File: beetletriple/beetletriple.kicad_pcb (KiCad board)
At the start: 4 copper layers, 80 x 70 mm, 65 parts, among them J1 Power IN, J2 motor_out, J3 motor_out, J4 motor_out, J5 input_c1, J6 input_c2, J7 input_c3, Q1 IRF8313PBF, Q2 IRF8313PBF, Q3 IRF8313PBF, Q4 IRF8313PBF, Q5 IRF8313PBF, Q6 IRF8313PBF, U1 LM2596S-ADJ, U11 FAN7388MX, U12 FAN7388MX, U2 HT7550-1, U3 ATtiny1617-M

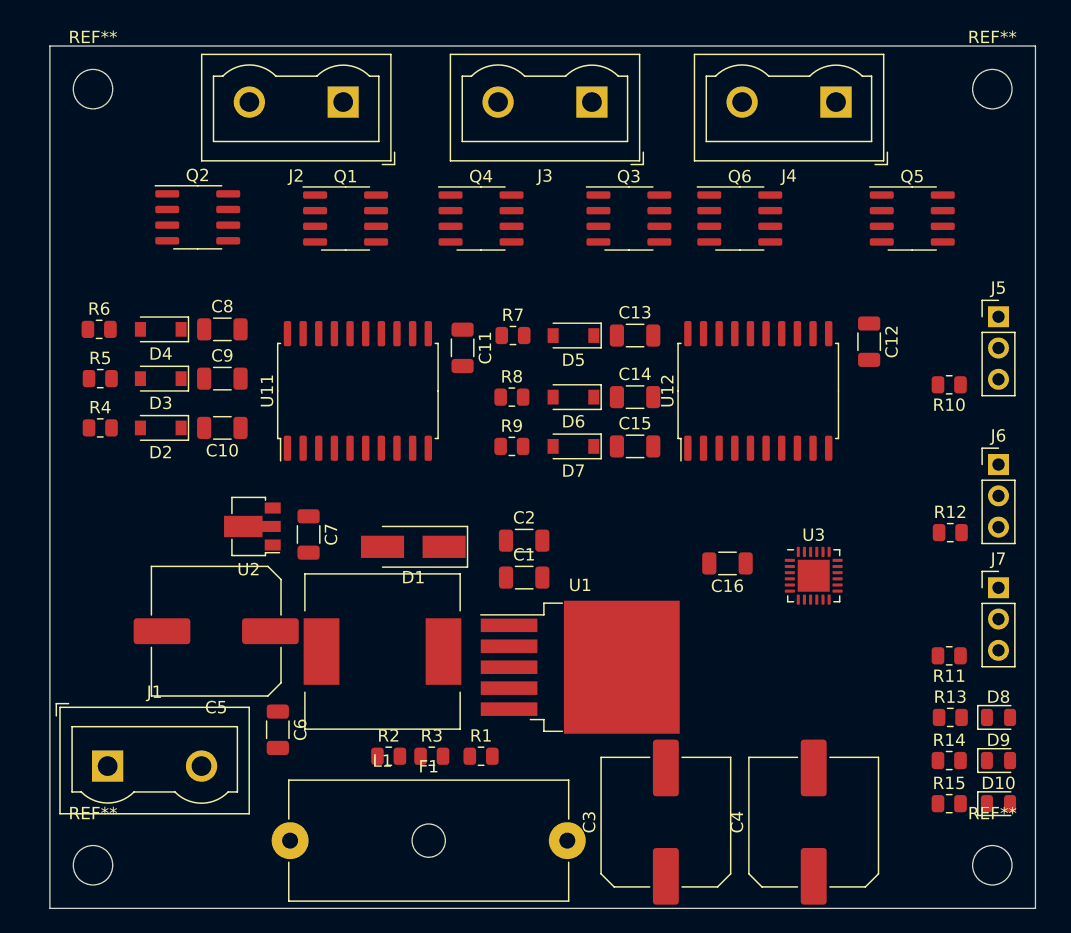
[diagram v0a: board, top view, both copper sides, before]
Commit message: Beetleweight triple esc
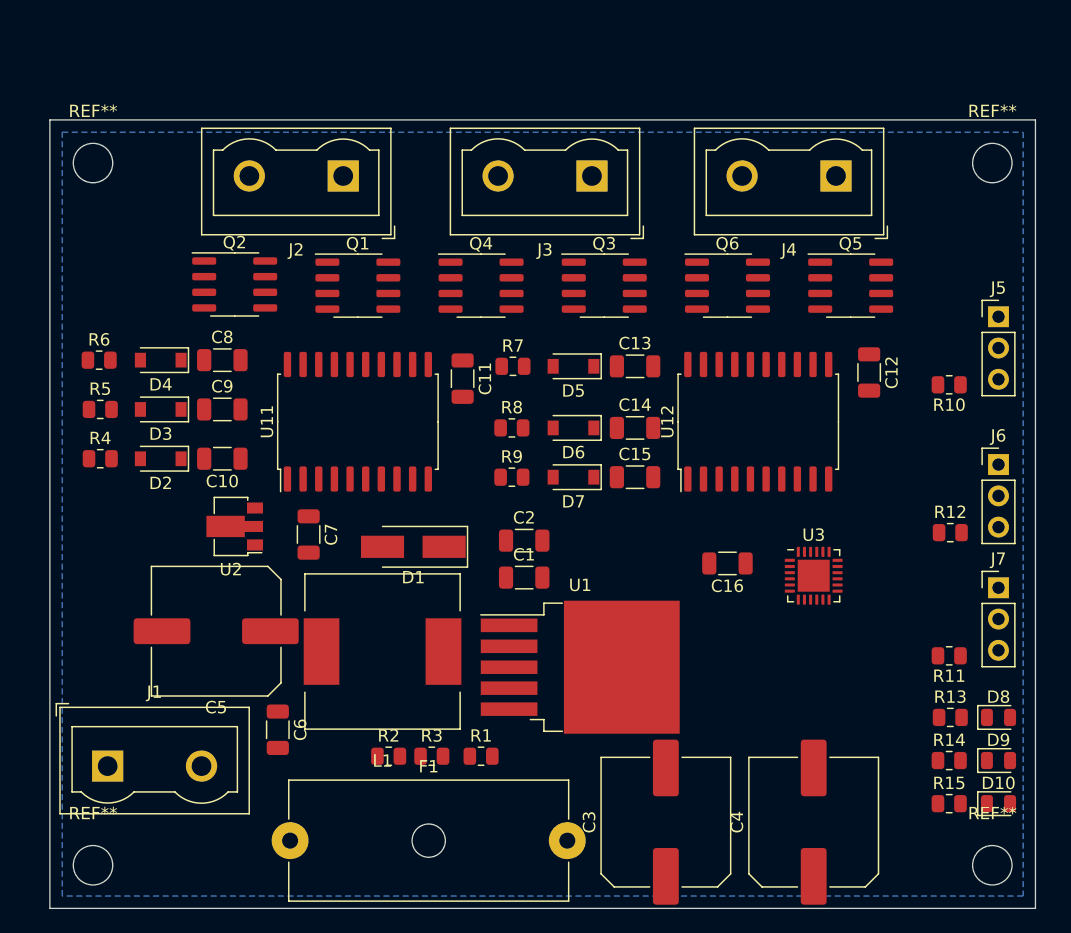
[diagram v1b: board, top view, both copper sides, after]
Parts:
- C10, C13, C14, C15, C8, C9: value C -> 2.2uF 50V
- C11, C12, C16: value 1uF 50V -> 2.2uF 50V
- R4, R5, R6, R7, R8, R9: value R -> 4.7R
- moved Q5 7.40 mm to (163.0, 89.5)
- moved Q2 6.22 mm to (113.0, 89.4)
- moved J2 6.00 mm to (121.8, 80.5)
- moved J3 6.00 mm to (142.0, 80.5)
- moved J4 6.00 mm to (161.8, 80.5)
- moved REF** 6.00 mm to (174.5, 79.5)
- moved REF** 6.00 mm to (101.5, 79.5)
- moved Q3 5.81 mm to (143.0, 89.5)
- moved Q1 5.54 mm to (123.0, 89.5)
- moved Q6 5.54 mm to (153.0, 89.5)
- moved Q4 5.45 mm to (133.0, 89.5)
- moved C10 2.50 mm to (112.0, 103.5)
- moved C11 2.50 mm to (131.5, 97.0)
- moved C12 2.50 mm to (164.5, 96.5)
- moved C13 2.50 mm to (145.5, 96.0)
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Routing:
- added copper zone on In1.Cu, net GND
- added copper zone on In2.Cu, net GND
- added copper zone on B.Cu, net VBAT
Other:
- board size 80 x 70 mm -> 80 x 64 mm

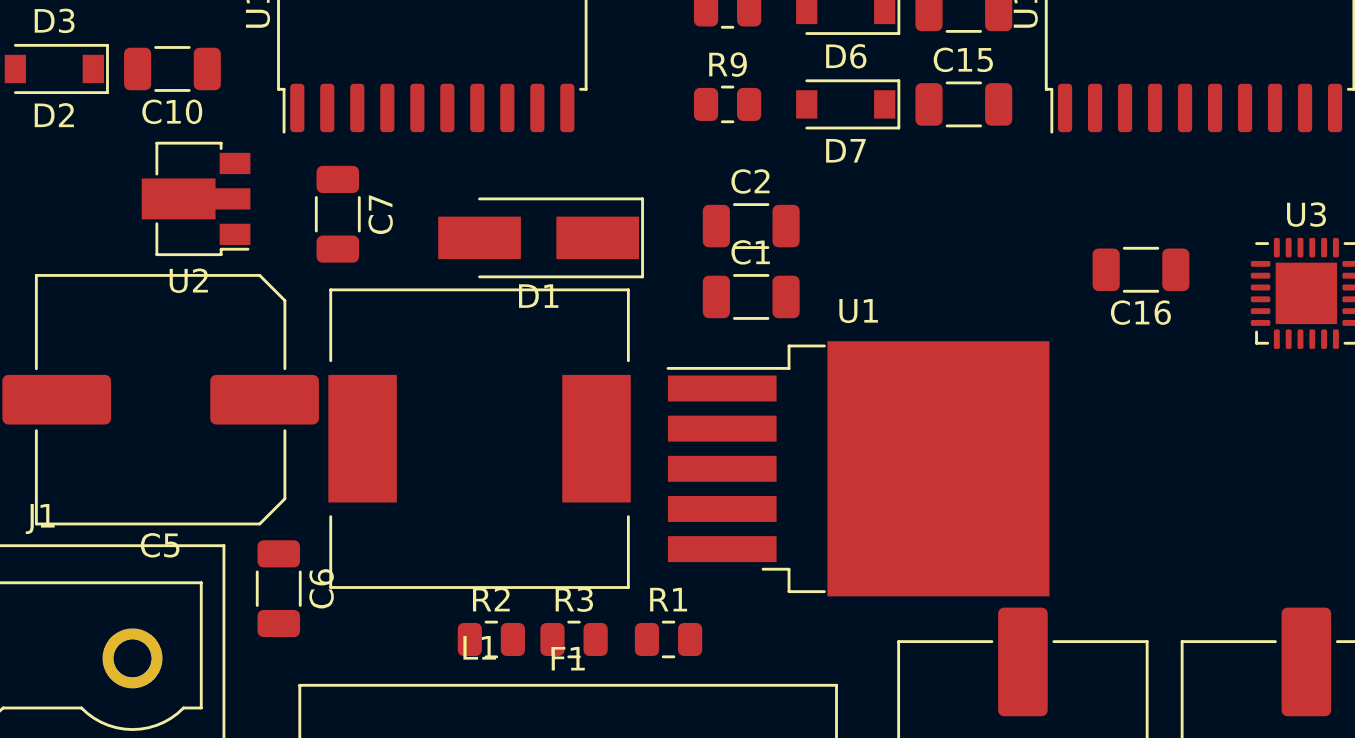
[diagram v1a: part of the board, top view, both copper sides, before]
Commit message: Beetleweight triple: redo the power and passives
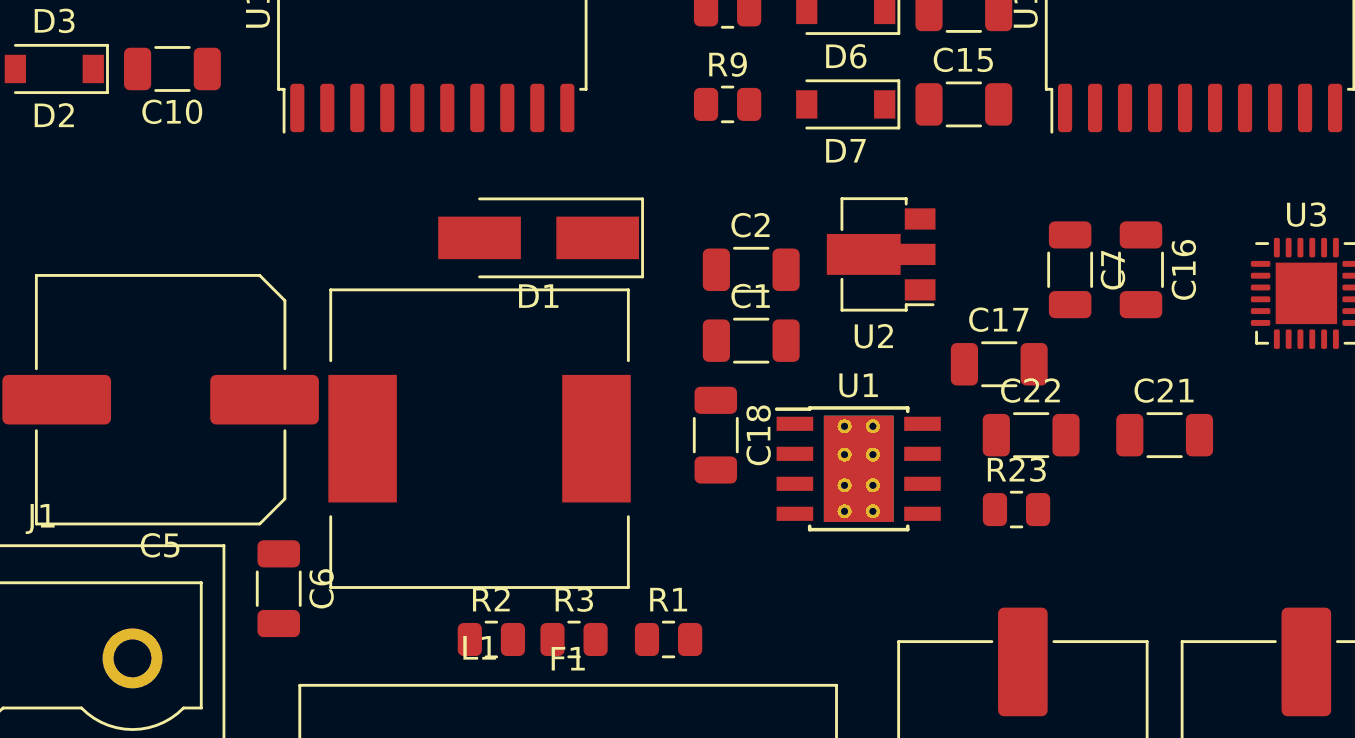
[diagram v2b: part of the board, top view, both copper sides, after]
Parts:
- added C17: 10nF, Capacitor_SMD:C_1206_3216Metric, F.Cu at (147.0, 116.0)
- added C18: 0.1uF, Capacitor_SMD:C_1206_3216Metric, F.Cu at (135.0, 119.0)
- added C21: DNP, Capacitor_SMD:C_1206_3216Metric, F.Cu at (154.0, 119.0)
- added C22: DNP, Capacitor_SMD:C_1206_3216Metric, F.Cu at (148.3, 119.0)
- added R23: DNP, Resistor_SMD:R_0805_2012Metric, F.Cu at (147.7, 122.2)
- L1: value 100uH -> 68uH
- R1: value 1k -> 10k
- R10, R11, R12: value 1k -> 1.5k
- R3: value 2.2k -> 100R
- U1: value LM2596S-ADJ -> TPS54331DR; footprint Package_TO_SOT_SMD:TO-263-5_TabPin3 -> Package_SO:TI_SO-PowerPAD-8_ThermalVias
- moved C7 31.1 mm to (150.0, 112.0)
- moved U2 29.1 mm to (142.0, 111.3)
- moved C1 1.85 mm to (136.5, 115.0)
- moved C2 1.85 mm to (136.5, 112.0)
- turned C16 to -90 degrees
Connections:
- R1 pad 1: Net-(R1-Pad1) -> VBEC
- R1 pad 2: GND -> Net-(R2-Pad1)
- R2 pad 1: VBEC -> Net-(R2-Pad1)
- R3 pad 2: Net-(R1-Pad1) -> GND
- U1 pad 1: VBAT -> Net-(C18-Pad1)
- U1 pad 2: /Power/SWITCH -> VBAT
- U1 pad 3: GND -> /Power/SWITCH
- U1 pad 4: Net-(R1-Pad1) -> GND
- U1 pad 5: GND -> Net-(R2-Pad1)

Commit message: Beetleweight triple: more.
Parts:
- added J8: output_c4, Connector_PinHeader_2.54mm:PinHeader_1x03_P2.54mm_Vertical, F.Cu at (175.5, 101.0)
- added J9: output_c5, Connector_PinHeader_2.54mm:PinHeader_1x03_P2.54mm_Vertical, F.Cu at (175.5, 105.5)
- L1: value 68uH -> 10uH
- moved J5 28.8 mm to (175.5, 120.8), turned to -90 degrees
- moved R10 23.9 mm to (166.5, 121.0)
- moved U3 22.1 mm to (138.0, 111.5), turned to -45 degrees
- moved C16 21.7 mm to (132.0, 117.5)
- moved U2 17.4 mm to (154.0, 124.0), turned to -90 degrees
- moved C21 15.2 mm to (140.0, 125.0)
- moved J6 14.2 mm to (175.5, 118.2), turned to -90 degrees
- moved C2 13.7 mm to (144.0, 123.5), turned to 90 degrees
- moved C1 13.5 mm to (147.0, 123.5), turned to 90 degrees
- moved R23 12.7 mm to (135.0, 122.0)
- moved C22 12.3 mm to (140.0, 128.0)
- moved C7 11.5 mm to (150.0, 123.5)
- moved U1 10.1 mm to (133.0, 126.5)
- moved R12 9.82 mm to (166.4, 118.1)
- moved C17 9.01 mm to (139.5, 121.0)
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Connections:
- net /Power/SWITCH renamed /Power/REG_PH
- net Net-(C17-Pad1) renamed /Power/REG_SOFTSTART
- net Net-(C18-Pad1) renamed /Power/REG_BOOT
- net Net-(C22-Pad1) renamed /Power/COMP
- net Net-(R2-Pad1) renamed /Power/REG_SENSE
- C10 pad 2: /Drivers/M2S1 -> /Drivers/M2S2
- C15 pad 2: /Drivers/M2S2 -> /Drivers/M2S1
- U11 pad 5: MOTOR2H1 -> MOTOR2H2
- U11 pad 6: MOTOR2L1 -> MOTOR2L2
- U11 pad 7: /Drivers/M2L1 -> /Drivers/M2L2
- U11 pad 8: /Drivers/M2S1 -> /Drivers/M2S2
- U11 pad 9: /Drivers/M2H1 -> /Drivers/M2H2
- U12 pad 1: MOTOR2H2 -> MOTOR2H1
- U12 pad 17: /Drivers/M2L2 -> /Drivers/M2L1
- U12 pad 18: /Drivers/M2S2 -> /Drivers/M2S1
- U12 pad 19: /Drivers/M2H2 -> /Drivers/M2H1
- U12 pad 2: MOTOR2L2 -> MOTOR2L1
- U3 pad 10: MOTOR3L1 -> MOTOR1L1
- U3 pad 11: MOTOR3H1 -> MOTOR1H1
- U3 pad 12: MOTOR2L2 -> MOTOR3L2
- U3 pad 13: MOTOR2H2 -> MOTOR3H2
- U3 pad 14: MOTOR2L1 -> MOTOR3L1
- U3 pad 15: MOTOR2H1 -> MOTOR3H1
- U3 pad 16: MOTOR1L2 -> MOTOR2L1
- U3 pad 17: MOTOR3L2 -> MOTOR2H1
- U3 pad 19: unconnected-(U3-Pad19) -> /MCU/SERVO2
- U3 pad 20: unconnected-(U3-Pad20) -> /MCU/SERVO1
- U3 pad 6: MOTOR1H1 -> MOTOR2L2
- U3 pad 7: MOTOR1L1 -> MOTOR2H2
- U3 pad 8: MOTOR1H2 -> MOTOR1L2
- U3 pad 9: MOTOR3H2 -> MOTOR1H2
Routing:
- net GND: track 0.00 -> 30.9 mm, vias 0 -> 16
- net VBAT: track 0.00 -> 24.8 mm, vias 0 -> 39
- net /Drivers/M1S2: track 0.00 -> 15.9 mm
- added copper zone on F.Cu, net /Drivers/M1S1
- added copper zone on F.Cu, net /Drivers/M1S2
- added copper zone on F.Cu, net /Drivers/M2S1
- added copper zone on F.Cu, net /Drivers/M2S2
- added copper zone on F.Cu, net /Drivers/M3S1
- added copper zone on F.Cu, net /Drivers/M3S2
- added copper zone on F.Cu, net VBAT
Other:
- board text added: "<- +5v"
- board text added: "<- GND"
- board text added: "<- SIG"
- board text added: "IN1"
- board text added: "IN2"
- board text added: "IN3"
- board text added: "OUT4"
- board text added: "OUT5"

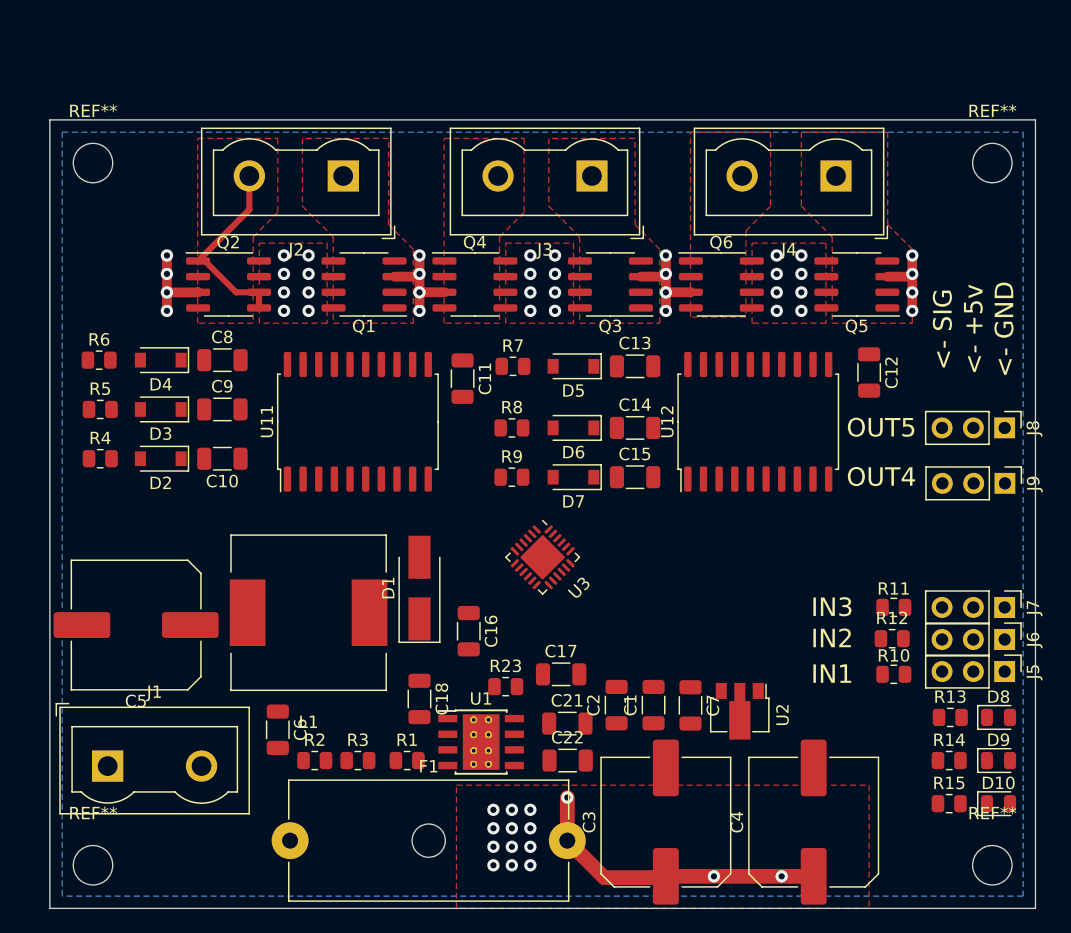
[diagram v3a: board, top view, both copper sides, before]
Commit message: Pin swaps and routing
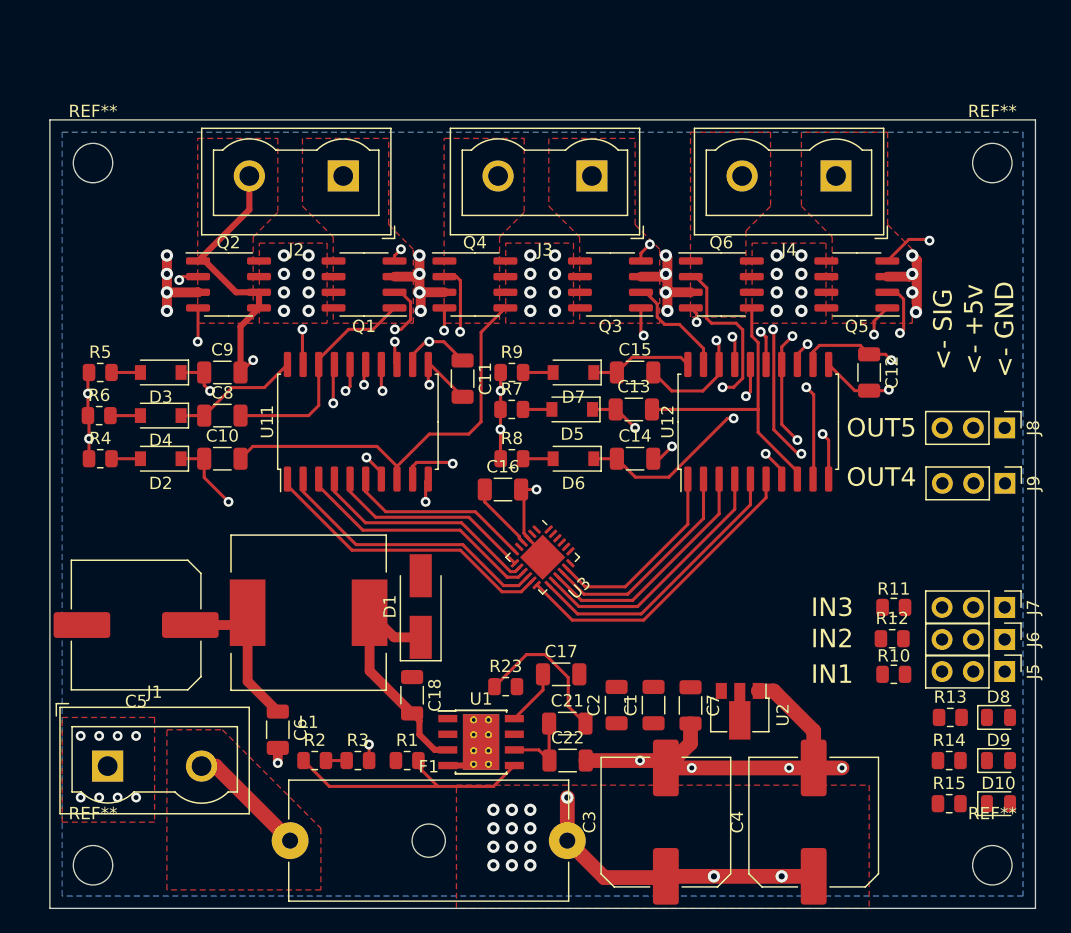
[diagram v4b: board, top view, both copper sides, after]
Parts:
- moved C16 11.8 mm to (134.8, 106.0), turned to 0 degrees
- moved C15 8.50 mm to (145.5, 96.5)
- moved D7 8.50 mm to (140.5, 96.5)
- moved R9 8.50 mm to (135.5, 96.5)
- moved C8 4.50 mm to (112.0, 100.0)
- moved D4 4.50 mm to (107.0, 100.0)
- moved R6 4.50 mm to (102.0, 100.0)
- moved C13 3.50 mm to (145.4, 99.5)
- moved D5 3.50 mm to (140.4, 99.5)
- moved R7 3.50 mm to (135.5, 99.5)
- moved C9 3.00 mm to (112.0, 96.5)
- moved D3 3.00 mm to (107.0, 96.5)
- moved R5 3.00 mm to (102.1, 96.5)
- moved C14 2.50 mm to (145.5, 103.5)
- moved D6 2.50 mm to (140.5, 103.5)
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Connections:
- C14 pad 2: /Drivers/H3S1 -> /Drivers/M3S1
- U12 pad 14: /Drivers/H3S1 -> /Drivers/M3S1
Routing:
- net GND: track 30.9 -> 89.1 mm, vias 16 -> 33
- net /Drivers/M2S2: track 0.00 -> 33.2 mm
- net /Drivers/M3S1: track 0.00 -> 31.1 mm, vias 0 -> 4
- net VBAT: track 24.8 -> 52.9 mm, vias 39 -> 45
- net /Drivers/M3H2: track 0.00 -> 27.8 mm, vias 0 -> 2
- net MOTOR3L2: track 0.00 -> 25.4 mm
- net /Drivers/M1H2: track 0.00 -> 25.4 mm, vias 0 -> 2
- net /Drivers/M3L2: track 0.00 -> 24.6 mm, vias 0 -> 4
- net MOTOR1H1: track 0.00 -> 24.4 mm
- net Net-(C10-Pad1): track 0.00 -> 24.1 mm, vias 0 -> 2
- net /Drivers/M3L1: track 0.00 -> 24.1 mm, vias 0 -> 2
- net /Drivers/M3S2: track 0.00 -> 24.0 mm
- net Net-(C13-Pad1): track 0.00 -> 23.4 mm, vias 0 -> 2
- net MOTOR3H2: track 0.00 -> 23.1 mm
- net /Drivers/M1L1: track 0.00 -> 22.8 mm, vias 0 -> 2
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- added copper zone on F.Cu, net GND
- added copper zone on F.Cu, net VBAT_IN_1

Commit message: Add new power in connector
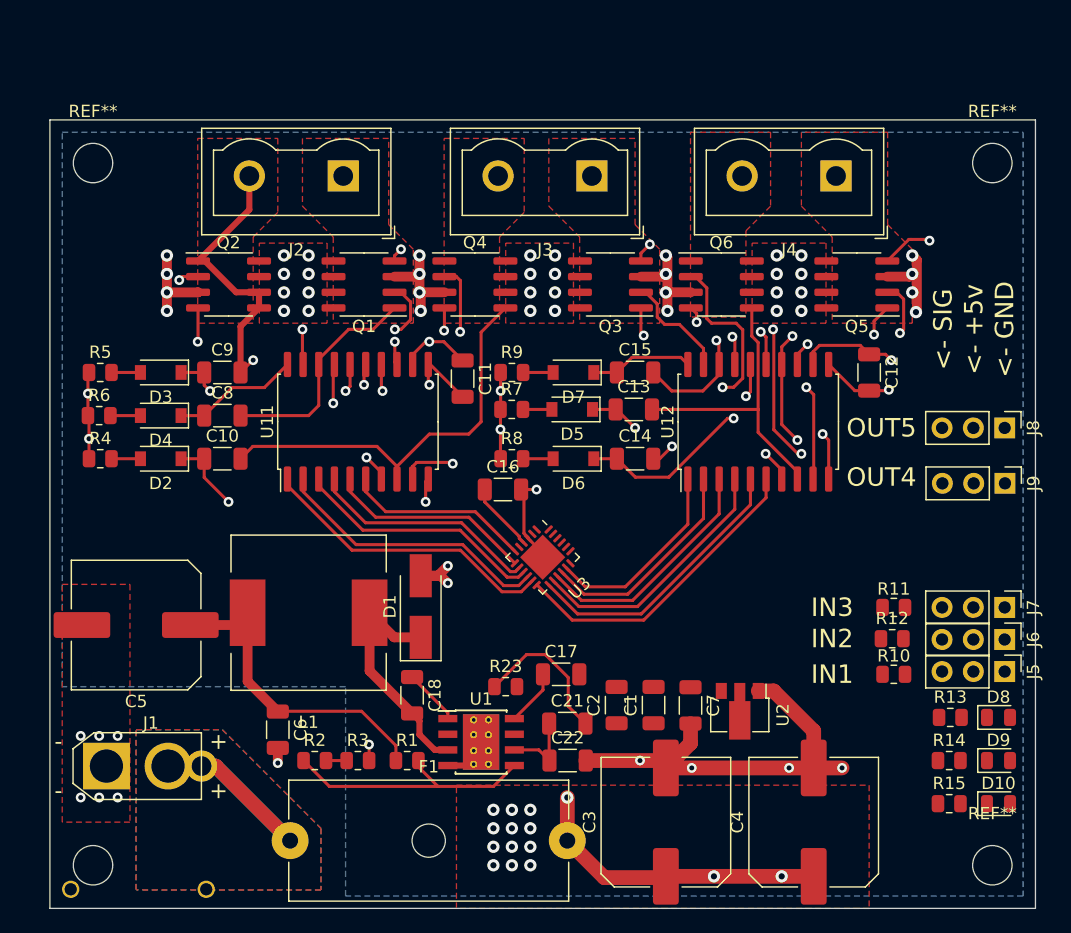
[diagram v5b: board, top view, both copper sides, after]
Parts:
- J1: footprint TerminalBlock:TerminalBlock_Wuerth_691311400102_P7.62mm -> beetletriple:beetlepower
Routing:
- net VBAT_IN_1: track 9.70 -> 22.1 mm
- net VBEC: track 14.1 -> 26.1 mm
- net GND: track 89.1 -> 94.1 mm
- net /Power/REG_BOOT: track 0.00 -> 4.57 mm
- added copper zone on B.Cu, net VBAT_IN_1
